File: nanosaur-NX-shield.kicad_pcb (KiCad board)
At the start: 2 copper layers, 11 parts, among them J1 Conn_01x04, J2 jetson_nano, J3 Conn_01x04, J4 Conn_01x04, J5 Conn_01x04, J7 Conn_01x06

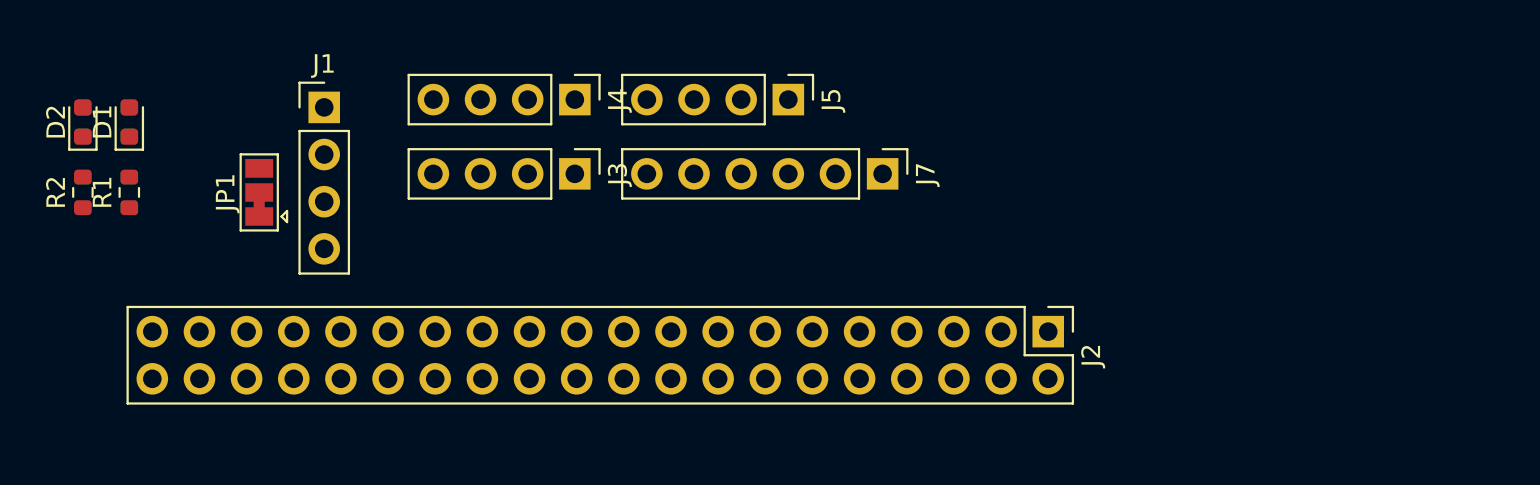
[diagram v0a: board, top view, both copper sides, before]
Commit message: Improve schematics and PCB
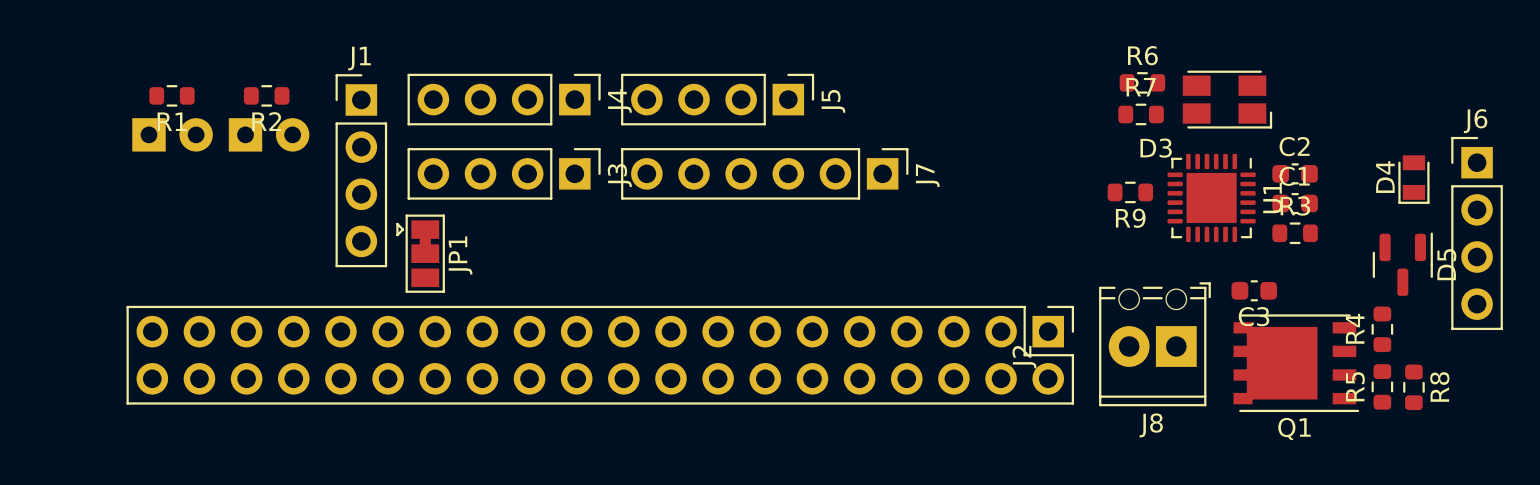
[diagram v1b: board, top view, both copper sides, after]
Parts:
- added C1: 1uF, Capacitor_SMD:C_0603_1608Metric, F.Cu at (148.3, 58.1)
- added C2: 1uF, Capacitor_SMD:C_0603_1608Metric, F.Cu at (148.3, 56.5)
- added C3: 1uF, Capacitor_SMD:C_0603_1608Metric, F.Cu at (146.1, 62.8)
- added D3: ASMB-MTB0-0A3A2, LED_SMD:LED_Avago_PLCC4_3.2x2.8mm_CW, F.Cu at (144.5, 52.5)
- added D4: ESDA25P35, Diode_SMD:D_MicroMELF, F.Cu at (154.7, 56.7)
- added D5: ESDA25W, Package_TO_SOT_SMD:SOT-23, F.Cu at (154.1, 61.4)
- added J6: Conn_01x04, Connector_PinHeader_2.54mm:PinHeader_1x04_P2.54mm_Vertical, F.Cu at (158.1, 55.9)
- added J8: Screw_Terminal_01x02, TerminalBlock_Phoenix:TerminalBlock_Phoenix_MPT-0,5-2-2.54_1x02_P2.54mm_Horizontal, F.Cu at (141.9, 65.8)
- added Q1: STL6P3LLH6, Package_SO:PowerPAK_SO-8_Single, F.Cu at (148.3, 66.7)
- added R3: 1k, Resistor_SMD:R_0603_1608Metric, F.Cu at (148.3, 59.7)
- added R4: 100k, Resistor_SMD:R_0603_1608Metric, F.Cu at (153.0, 64.9)
- added R5: 22k, Resistor_SMD:R_0603_1608Metric, F.Cu at (153.0, 68.0)
- added R6: 22k, Resistor_SMD:R_0603_1608Metric, F.Cu at (140.1, 51.6)
- added R7: 22k, Resistor_SMD:R_0603_1608Metric, F.Cu at (140.0, 53.3)
- added R8: 100, Resistor_SMD:R_0603_1608Metric, F.Cu at (154.7, 68.0)
- added R9: 1k, Resistor_SMD:R_0603_1608Metric, F.Cu at (139.4, 57.5)
- added U1: STUSB4500QTR, Package_DFN_QFN:QFN-24-1EP_4x4mm_P0.5mm_EP2.7x2.7mm, F.Cu at (143.8, 57.8)
- D1, D2: footprint LED_SMD:LED_0603_1608Metric -> LED_THT:LED_D3.0mm_Horizontal_O1.27mm_Z2.0mm; moved to B.Cu
- moved R2 11.2 mm to (92.9, 52.3), turned to 180 degrees
- moved JP1 9.53 mm to (101.4, 60.8), turned to -90 degrees
- moved D2 8.79 mm to (91.8, 54.4), turned to 0 degrees
- moved R1 5.69 mm to (87.8, 52.3), turned to 180 degrees
- moved J1 2.04 mm to (98.0, 52.5)
- moved D1 1.26 mm to (86.6, 54.4), turned to 0 degrees
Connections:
- net Net-(J2-Pad27) renamed SDA1
- net Net-(J2-Pad28) renamed SCL1
- net Net-(J2-Pad3) renamed SDA2
- net Net-(J2-Pad5) renamed SCL2
- J2 pad 11: Net-(J2-Pad11) -> unconnected-(J2-Pad11)
- J2 pad 12: Net-(J2-Pad12) -> unconnected-(J2-Pad12)
- J2 pad 13: Net-(J2-Pad13) -> unconnected-(J2-Pad13)
- J2 pad 15: Net-(J2-Pad15) -> unconnected-(J2-Pad15)
- J2 pad 16: Net-(J2-Pad16) -> unconnected-(J2-Pad16)
- J2 pad 18: Net-(J2-Pad18) -> unconnected-(J2-Pad18)
- J2 pad 19: Net-(J2-Pad19) -> unconnected-(J2-Pad19)
- J2 pad 21: Net-(J2-Pad21) -> unconnected-(J2-Pad21)
- J2 pad 22: Net-(J2-Pad22) -> unconnected-(J2-Pad22)
- J2 pad 23: Net-(J2-Pad23) -> unconnected-(J2-Pad23)
- J2 pad 24: Net-(J2-Pad24) -> unconnected-(J2-Pad24)
- J2 pad 26: Net-(J2-Pad26) -> unconnected-(J2-Pad26)
- J2 pad 29: Net-(J2-Pad29) -> unconnected-(J2-Pad29)
- J2 pad 32: Net-(J2-Pad32) -> unconnected-(J2-Pad32)
- J2 pad 35: Net-(J2-Pad35) -> unconnected-(J2-Pad35)
- J2 pad 36: Net-(J2-Pad36) -> unconnected-(J2-Pad36)
- J2 pad 37: Net-(J2-Pad37) -> unconnected-(J2-Pad37)
- J2 pad 38: Net-(J2-Pad38) -> unconnected-(J2-Pad38)
- J2 pad 40: Net-(J2-Pad40) -> unconnected-(J2-Pad40)
- J2 pad 7: Net-(J2-Pad7) -> unconnected-(J2-Pad7)
- J7 pad 1: Net-(J7-Pad1) -> unconnected-(J7-Pad1)
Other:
- net class Default removed
